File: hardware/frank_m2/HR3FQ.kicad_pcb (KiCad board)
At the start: 2 copper layers, 99 x 80.1 mm, 108 parts, among them CON1 Pin Header 1x03, CON2 Pin Header 1x03, CON3 Pin Header 1x08, J1 Pin Header 2x18, Q1 BC850, Q2 BC850, U1 NCP1117 3.3

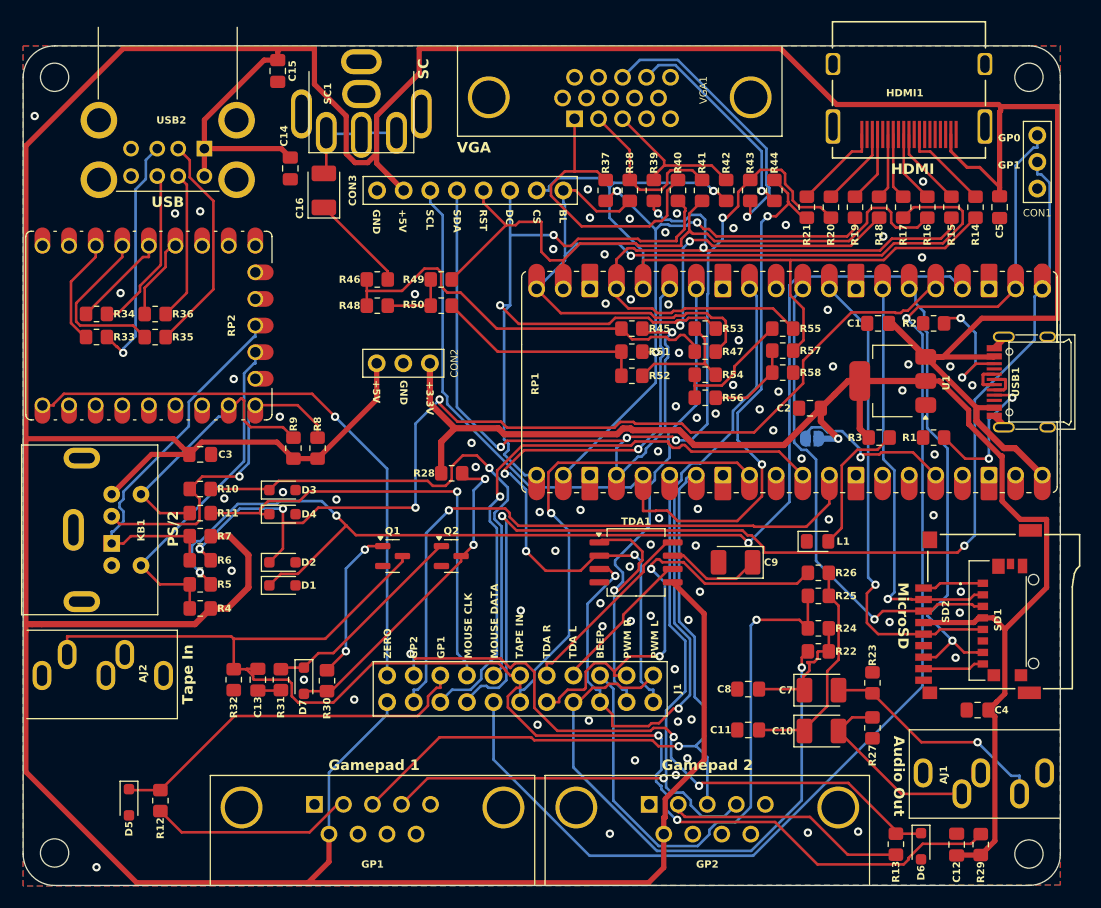
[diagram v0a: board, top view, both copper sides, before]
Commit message: Fixed tape loading bug on all PCBs
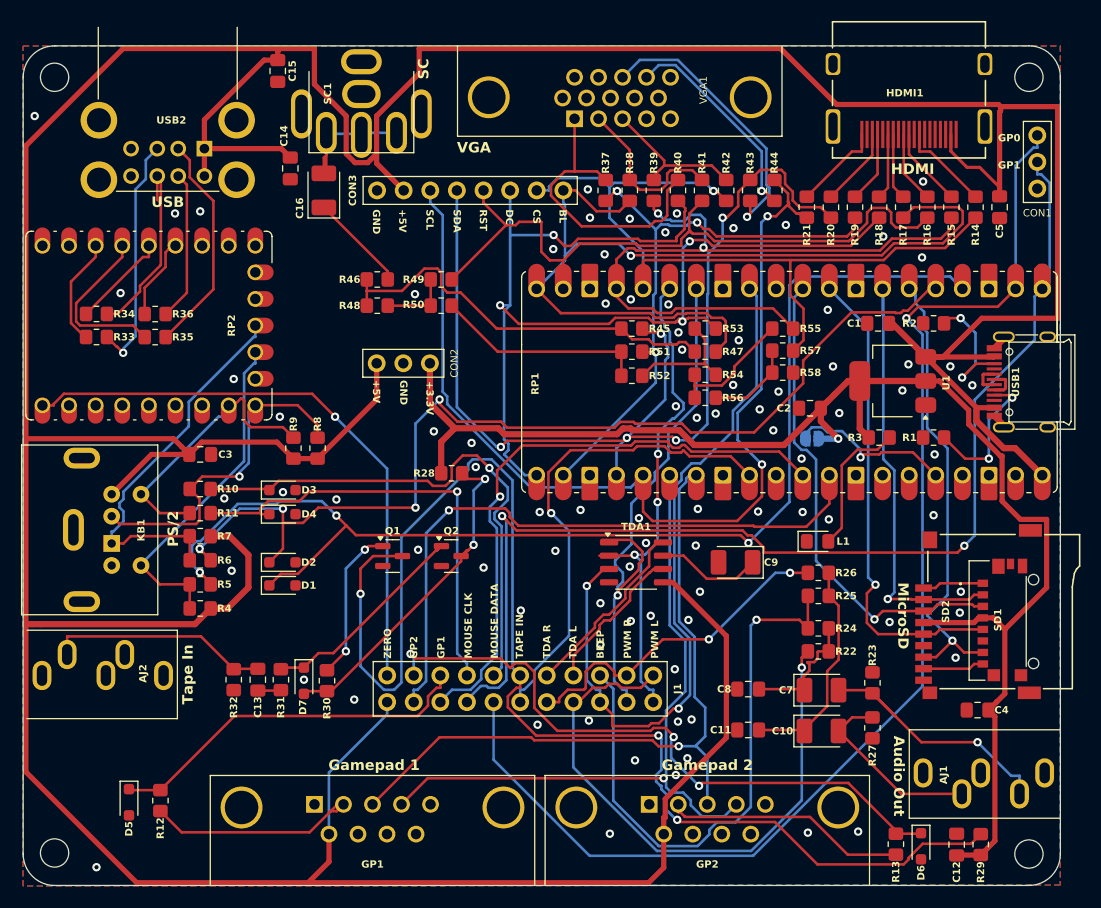
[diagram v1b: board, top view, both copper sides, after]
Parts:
- TDA1: footprint FRANK:SOIC-8 -> FRANK:SO-8
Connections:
- net /Zero/ZGPIO0_1 renamed /Zero/ZGPIO0
- net /Zero/ZGPIO1 renamed /Zero/ZGPIO1_1
- net /Zero/ZGPIO10_1 renamed /Zero/ZGPIO10
- net /Zero/ZGPIO26_1 renamed /Zero/ZGPIO26
- net /Zero/ZGPIO28 renamed /Zero/ZGPIO28_1
- net /Zero/ZGPIO6 renamed /Zero/ZGPIO6_1
- net /Zero/ZGPIO7 renamed /Zero/ZGPIO7_1
- net /Zero/ZGPIO8_1 renamed /Zero/ZGPIO8
- net /Zero/ZGPIO9_1 renamed /Zero/ZGPIO9
- AJ2 pad T: /LOAD_IN_D -> Net-(AJ2-PadT)
- C13 pad 1: /LOAD_IN_D -> Net-(AJ2-PadT)
- R32 pad 1: /LOAD_IN_D -> Net-(AJ2-PadT)
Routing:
- net Net-(AJ2-PadT): track 0.00 -> 21.2 mm
- net /GPIO11: track 65.7 -> 49.2 mm, vias 4 -> 3
- net /A_OUTR: track 42.0 -> 32.4 mm
- net /LOAD_IN_D: track 133.6 -> 127.2 mm, vias 2 -> 3
- net VBUS: track 489.5 -> 493.8 mm
- net /GPIO5: track 39.6 -> 43.6 mm
- net /Audio Out/L: track 22.0 -> 25.5 mm
- net /GPIO22: track 45.0 -> 48.0 mm
- net /GPIO18: track 106.1 -> 103.2 mm
- net Net-(USB2-D2+): track 15.5 -> 18.3 mm
- net /GPIO3: track 97.0 -> 99.6 mm
- net /GPIO19: track 94.3 -> 96.9 mm
- net /GPIO4: track 43.4 -> 46.0 mm
- net /Composite/CVBS: track 10.1 -> 12.5 mm
- net /GPIO6: track 45.2 -> 47.3 mm
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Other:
- board text added: "HW Revision 1.03 (M2)"
- board text removed: "HW Revision 1.02 (M2)"

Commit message: Minor updates
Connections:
- net /Pico/5V_PICO_1 renamed /Pico/5V_PICO
- net /Pico/GPIO23 renamed /Pico/GPIO23_1
- net /Pico/GPIO28_1 renamed /Pico/GPIO28
- net /Pico/GPIO29_1 renamed /Pico/GPIO29
- net /Pico/GPIO8_1 renamed /Pico/GPIO8
- net /Pico/RUN renamed /Pico/RUN_1
- net /Zero/ZGPIO0 renamed /Zero/ZGPIO0_1
- net /Zero/ZGPIO10 renamed /Zero/ZGPIO10_1
- net /Zero/ZGPIO13 renamed /Zero/ZGPIO13_1
- net /Zero/ZGPIO1_1 renamed /Zero/ZGPIO1
- net /Zero/ZGPIO26 renamed /Zero/ZGPIO26_1
- net /Zero/ZGPIO27_1 renamed /Zero/ZGPIO27
- net /Zero/ZGPIO28_1 renamed /Zero/ZGPIO28
- net /Zero/ZGPIO29 renamed /Zero/ZGPIO29_1
- net /Zero/ZGPIO6_1 renamed /Zero/ZGPIO6
- net /Zero/ZGPIO7_1 renamed /Zero/ZGPIO7
- net /Zero/ZGPIO8 renamed /Zero/ZGPIO8_1
- net /Zero/ZGPIO9 renamed /Zero/ZGPIO9_1

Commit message: Minor updates
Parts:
- renumbered C11 to C10, C12 to C11, C13 to C12, C14 to C13, C15 to C14, C16 to C15, C7 to C6, C8 to C7, C9 to C8, C10 to C9, CON1 to J1, AJ1 to J10, AJ2 to J11, USB2 to J12, VGA1 to J13, CON3 to J14, SC1 to J15, CON2 to J2, USB1 to J3, KB1 to J4, SD1 to J5, SD2 to J6, GP1 to J7, GP2 to J8, HDMI1 to J9, J1 to JP1, L1 to LD1, TDA1 to U2, RP1 to U3, RP2 to U4
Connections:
- net /Pico/5V_PICO renamed /Pico/5V_PICO_1
- net /Pico/GPIO28 renamed /Pico/GPIO28_1
- net /Pico/GPIO8 renamed /Pico/GPIO8_1
- net /Pico/RUN_1 renamed /Pico/RUN
- net /Zero/ZGPIO0_1 renamed /Zero/ZGPIO0
- net /Zero/ZGPIO10_1 renamed /Zero/ZGPIO10
- net /Zero/ZGPIO26_1 renamed /Zero/ZGPIO26
- net /Zero/ZGPIO28 renamed /Zero/ZGPIO28_1
- net /Zero/ZGPIO29_1 renamed /Zero/ZGPIO29
- net /Zero/ZGPIO6 renamed /Zero/ZGPIO6_1
- J10 pad RN: /Audio Out/R* -> (no net)
- J10 pad TN: /Audio Out/L* -> (no net)
- J11 pad RN: unconnected-(AJ2-PadRN) -> (no net)
- J11 pad TN: unconnected-(AJ2-PadTN) -> (no net)
